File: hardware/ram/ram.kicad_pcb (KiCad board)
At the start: 4 copper layers, 102.9 x 133.3 mm, 64 parts, among them J1 I/O Expansion 1, J2 I/O Expansion 2, J3 DB25_Male, J4 DB37_Male, U1 71V016SA12PHGI, U10 SN74HCS00PWR, U11 SN74HCS00PWR, U12 SN74HCS00PWR, U13 SN74HCS00PWR, U14 SN74HCS00PWR, U15 SN74HCS00PWR, U16 SN74HCS00PWR, U17 SN74HCS00PWR, U18 SN74HCS00PWR, U19 SN74HCS00PWR, U2 SN74HCS00PWR, U20 SN74HCS00PWR, U21 SN74HCS00PWR, U22 SN74HCS00PWR, U23 SN74HCS00PWR, U24 SN74HCS00PWR, U25 SN74HCS00PWR, U26 SN74HCS00PWR, U27 SN74HCS00PWR, U28 SN74HCS00PWR, U29 SN74HCS00PWR, U3 SN74HCS00PWR, U30 SN74HCS00PWR, U31 SN74HCS00PWR, U32 SN74HCS00PWR, U33 SN74HCS00PWR, U34 SN74HCS00PWR, U35 SN74HCS00PWR, U36 SN74HCS00PWR, U37 SN74HCS00PWR, U38 SN74HCS00PWR, U39 SN74HCS00PWR, U4 SN74HCS00PWR, U40 SN74HCS00PWR, U41 SN74HCS00PWR, U42 SN74HCS00PWR, U43 SN74HCS00PWR, U44 SN74HCS00PWR, U45 SN74HCS00PWR, U46 SN74HCS00PWR, U47 SN74HCS00PWR, U48 SN74HCS00PWR, U49 SN74HCS00PWR, U5 SN74LVC541APWR, U50 SN74HCS00PWR, U51 SN74HCS00PWR, U52 SN74HCS00PWR, U53 SN74HCS00PWR, U54 SN74HCS00PWR, U6 SN74LVC541APWR, U7 SN74HCS00PWR, U8 SN74HCS00PWR, U9 SN74HCS00PWR

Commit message: All boards as fabbed at v1.0
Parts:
- added G***: LOGO, nandirl logo:logo_sm, F.Cu at (224.8, 16.5)

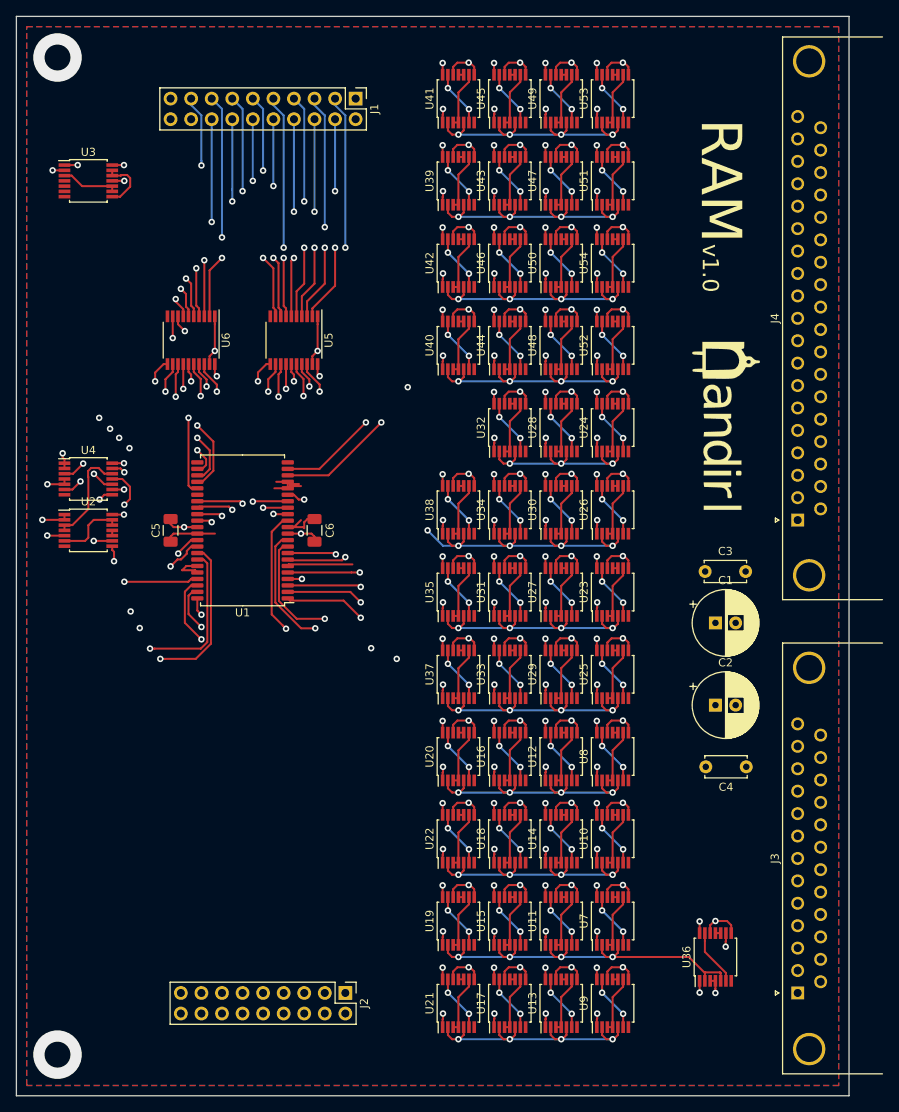
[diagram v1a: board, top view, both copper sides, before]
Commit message: RAM board rework complete. Added COTS latch chips and Teensy 4.1 peripheral + magjack for ethernet.
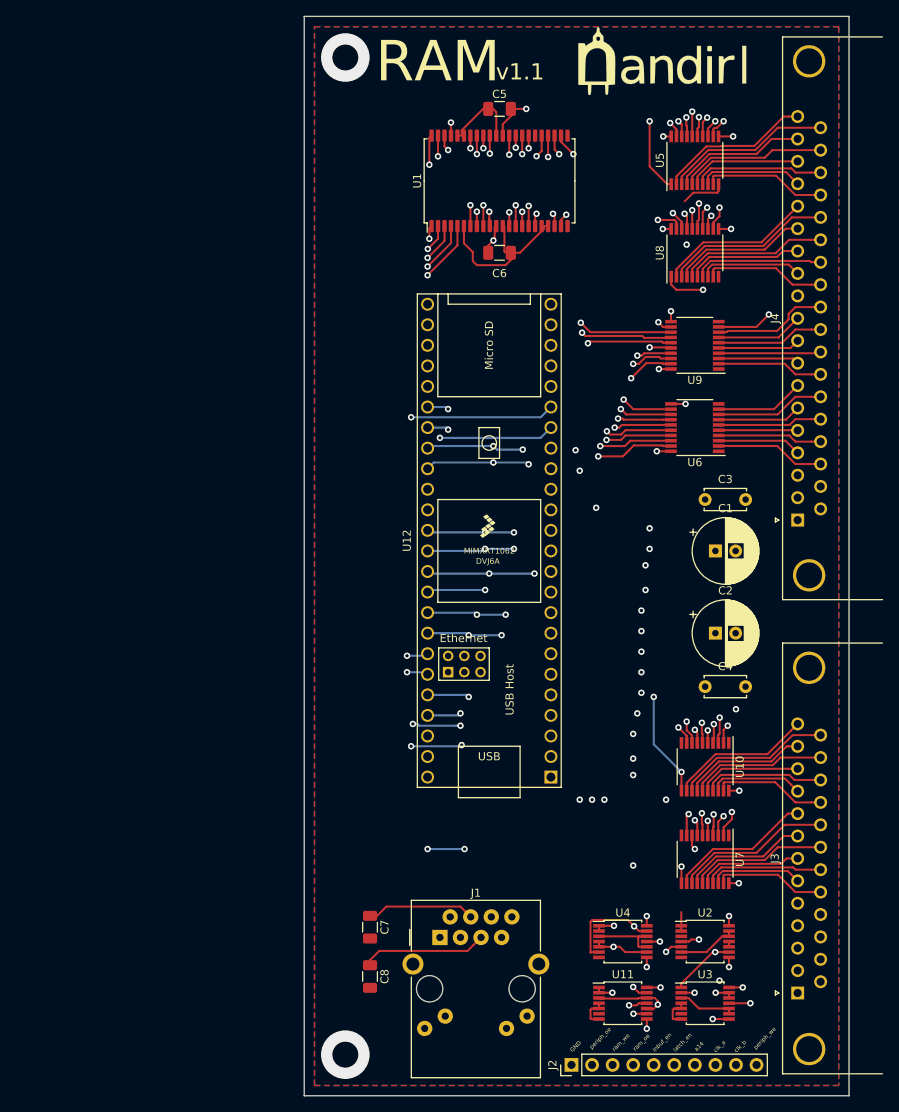
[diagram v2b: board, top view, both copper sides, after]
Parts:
- removed U13, U14, U15, U16, U17, U18, U19, U20, U21, U22, U23, U24, U25, U26, U27, U28, U29, U30, U31, U32, U33, U34, U35, U36, U37, U38, U39, U40, U41, U42, U43, U44, U45, U46, U47, U48, U49, U50, U51, U52, U53, U54: SN74HCS00PWR, Package_SO:TSSOP-14_4.4x5mm_P0.65mm
- added C7: 0.1uF, Capacitor_SMD:C_1206_3216Metric, F.Cu at (180.8, 78.2)
- added C8: 0.1uF, Capacitor_SMD:C_1206_3216Metric, F.Cu at (180.8, 84.3)
- J1: value I/O Expansion 1 -> RJ45_Amphenol_RJMG1BD3B8K1ANR; footprint Connector_PinHeader_2.54mm:PinHeader_2x10_P2.54mm_Vertical -> Connector_RJ:RJ45_Amphenol_RJMG1BD3B8K1ANR
- J2: value I/O Expansion 2 -> Conn_01x10_Male; footprint Connector_PinHeader_2.54mm:PinHeader_2x09_P2.54mm_Vertical -> Connector_PinHeader_2.54mm:PinHeader_1x10_P2.54mm_Vertical
- U10, U7, U8, U9: value SN74HCS00PWR -> 74LCX573FT; footprint Package_SO:TSSOP-14_4.4x5mm_P0.65mm -> Package_SO:TSSOP-20_4.4x6.5mm_P0.65mm
- U12: value SN74HCS00PWR -> Teensy4.1; footprint Package_SO:TSSOP-14_4.4x5mm_P0.65mm -> nandirl logo:Teensy41
- U5, U6: value SN74LVC541APWR -> 74LCX573FT
- moved U3 127.0 mm to (222.2, 87.6)
- moved J1 104.2 mm to (189.5, 79.5), turned to 0 degrees
- moved U2 91.6 mm to (222.2, 80.0)
- moved U4 87.3 mm to (212.1, 80.0)
- moved U9 81.9 mm to (221.0, 6.35), turned to 180 degrees
- moved C5 66.1 mm to (196.8, -22.9), turned to 0 degrees
- moved U6 63.2 mm to (221.0, 16.5), turned to 180 degrees
- moved U8 63.1 mm to (221.0, -5.08)
- moved U5 54.3 mm to (221.0, -16.5), turned to 90 degrees
- moved U1 53.6 mm to (196.8, -14.0), turned to 90 degrees
- moved G*** 45.8 mm to (217.2, -28.7), turned to 0 degrees
- moved C6 41.2 mm to (196.8, -5.08), turned to 0 degrees
- moved J2 29.3 mm to (205.7, 95.2), turned to 90 degrees
- moved U12 28.1 mm to (195.6, 30.5)
- moved U10 14.5 mm to (222.2, 58.4), turned to 270 degrees
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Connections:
- J1 pad 13: a10 -> Net-(J1-Pad13)
- J2 pad 1: io_0 -> GND
- J2 pad 10: io_9 -> periph_we
- J2 pad 2: io_1 -> periph_oe
- J2 pad 3: io_2 -> ram_we
- J2 pad 4: io_3 -> ram_oe
- J2 pad 5: io_4 -> inbuf_en
- J2 pad 6: io_5 -> latch_en
- J2 pad 7: io_6 -> a14
- J2 pad 8: io_7 -> clk_a
- J2 pad 9: io_8 -> clk_b
- U10 pad 1: io_8 -> GND
- U10 pad 10: Net-(U10-Pad10) -> GND
- U10 pad 11: Net-(U10-Pad10) -> latch_en
- U10 pad 12: out_8 -> out_15
- U10 pad 13: Net-(U10-Pad13) -> out_14
- U10 pad 14: +3V3 -> out_13
- U10 pad 2: latch_en -> io_8
- U10 pad 3: Net-(U10-Pad3) -> io_9
- U10 pad 4: Net-(U10-Pad3) -> io_10
- U10 pad 5: latch_en -> io_11
- U10 pad 6: Net-(U10-Pad13) -> io_12
- U10 pad 7: GND -> io_13
- U10 pad 8: out_8 -> io_14
- U10 pad 9: Net-(U10-Pad3) -> io_15
- U11 pad 1: io_5 -> clk_b
- U11 pad 10: Net-(U11-Pad10) -> latch_en
- U11 pad 11: Net-(U11-Pad10) -> periph_oe
- U11 pad 12: out_5 -> latch_en
- U11 pad 13: Net-(U11-Pad13) -> a14
- U11 pad 2: latch_en -> clk_b
- U11 pad 3: Net-(U11-Pad3) -> latch_en
- U11 pad 4: Net-(U11-Pad3) -> GND
- U11 pad 5: latch_en -> GND
- U11 pad 6: Net-(U11-Pad13) -> Net-(U11-Pad6)
- U11 pad 8: out_5 -> ram_oe
- U11 pad 9: Net-(U11-Pad3) -> /not_a14
- U12 pad 1: io_13 -> GND
- U12 pad 10: Net-(U12-Pad10) -> a8
- U12 pad 11: Net-(U12-Pad10) -> a9
- U12 pad 12: out_13 -> a10
- U12 pad 13: Net-(U12-Pad13) -> a11
- U12 pad 14: +3V3 -> a12
- U12 pad 2: latch_en -> a0
- U12 pad 3: Net-(U12-Pad3) -> a1
- U12 pad 4: Net-(U12-Pad3) -> a2
- U12 pad 5: latch_en -> a3
- U12 pad 6: Net-(U12-Pad13) -> a4
- U12 pad 7: GND -> a5
- U12 pad 8: out_13 -> a6
- U12 pad 9: Net-(U12-Pad3) -> a7
- U2 pad 1: a14 -> GND
- U2 pad 2: a14 -> GND
- U2 pad 3: /not_a14 -> Net-(U2-Pad3)
- U2 pad 4: /not_a14 -> clk_b
- U3 pad 4: Net-(U3-Pad4) -> GND
- U3 pad 5: Net-(U3-Pad5) -> GND
- U4 pad 11: ram_oe -> ram_we
- U4 pad 12: /not_a14 -> Net-(U4-Pad10)
- U4 pad 13: latch_en -> /not_a14
- U4 pad 4: clk_b -> a14
- U4 pad 5: clk_b -> a14
- U4 pad 6: latch_en -> /not_a14
- U4 pad 8: ram_we -> periph_we
- U4 pad 9: clk_b -> a14
- U5 pad 11: io_7 -> latch_en
- U5 pad 12: io_6 -> io_7
- U5 pad 13: io_5 -> io_6
- U5 pad 14: io_4 -> io_5
- U5 pad 15: io_3 -> io_4
- U5 pad 16: io_2 -> io_3
- U5 pad 17: io_1 -> io_2
- U5 pad 18: io_0 -> io_1
- U5 pad 19: inbuf_en -> io_0
- U5 pad 2: /input_latch/out0 -> in_0
- U5 pad 3: /input_latch/out1 -> in_1
- U5 pad 4: /input_latch/out2 -> in_2
- U5 pad 5: /input_latch/out3 -> in_3
- U5 pad 6: /input_latch/out4 -> in_4
- U5 pad 7: /input_latch/out5 -> in_5
- U5 pad 8: /input_latch/out6 -> in_6
- U5 pad 9: /input_latch/out7 -> in_7
- U6 pad 1: inbuf_en -> GND
- U6 pad 11: io_15 -> latch_en
- U6 pad 12: io_14 -> a7
- U6 pad 13: io_13 -> a6
- U6 pad 14: io_12 -> a5
- U6 pad 15: io_11 -> a4
- U6 pad 16: io_10 -> a3
- U6 pad 17: io_9 -> a2
- U6 pad 18: io_8 -> a1
- U6 pad 19: inbuf_en -> a0
- U6 pad 2: /input_latch/out8 -> addr_0
- U6 pad 3: /input_latch/out9 -> addr_1
- U6 pad 4: /input_latch/out10 -> addr_2
- U6 pad 5: /input_latch/out11 -> addr_3
- U6 pad 6: /input_latch/out12 -> addr_4
- U6 pad 7: /input_latch/out13 -> addr_5
- U6 pad 8: /input_latch/out14 -> addr_6
- U6 pad 9: /input_latch/out15 -> addr_7
- U7 pad 1: io_4 -> GND
- U7 pad 10: Net-(U7-Pad10) -> GND
- U7 pad 11: Net-(U7-Pad10) -> latch_en
- U7 pad 12: out_4 -> out_7
- U7 pad 13: Net-(U7-Pad13) -> out_6
- U7 pad 14: +3V3 -> out_5
- U7 pad 2: latch_en -> io_0
- U7 pad 3: Net-(U7-Pad3) -> io_1
- U7 pad 4: Net-(U7-Pad3) -> io_2
- U7 pad 5: latch_en -> io_3
- U7 pad 6: Net-(U7-Pad13) -> io_4
- U7 pad 7: GND -> io_5
- U7 pad 8: out_4 -> io_6
- U7 pad 9: Net-(U7-Pad3) -> io_7
- U8 pad 1: io_12 -> inbuf_en
- U8 pad 10: Net-(U8-Pad10) -> GND
- U8 pad 11: Net-(U8-Pad10) -> latch_en
- U8 pad 12: out_12 -> io_15
- U8 pad 13: Net-(U8-Pad13) -> io_14
- U8 pad 14: +3V3 -> io_13
- U8 pad 2: latch_en -> in_8
- U8 pad 3: Net-(U8-Pad3) -> in_9
- U8 pad 4: Net-(U8-Pad3) -> in_10
- U8 pad 5: latch_en -> in_11
- U8 pad 6: Net-(U8-Pad13) -> in_12
- U8 pad 7: GND -> in_13
- U8 pad 8: out_12 -> in_14
- U8 pad 9: Net-(U8-Pad3) -> in_15
- U9 pad 1: io_0 -> GND
- U9 pad 10: Net-(U9-Pad10) -> GND
- U9 pad 11: Net-(U9-Pad10) -> latch_en
- U9 pad 12: out_0 -> load
- U9 pad 13: Net-(U9-Pad13) -> a14
- U9 pad 14: +3V3 -> a13
- U9 pad 2: latch_en -> addr_8
- U9 pad 3: Net-(U9-Pad3) -> addr_9
- U9 pad 4: Net-(U9-Pad3) -> addr_10
- U9 pad 5: latch_en -> addr_11
- U9 pad 6: Net-(U9-Pad13) -> addr_12
- U9 pad 7: GND -> addr_13
- U9 pad 8: out_0 -> addr_14
- U9 pad 9: Net-(U9-Pad3) -> load_in
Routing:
- net latch_en: track 618.7 -> 144.7 mm, vias 50 -> 8
- net ram_oe: track 24.3 -> 138.6 mm, vias 2 -> 4
- net load: track 209.9 -> 99.7 mm, vias 2 -> 3
- net inbuf_en: track 54.9 -> 161.0 mm, vias 3 -> 4
- net periph_we: track 0.00 -> 102.7 mm, vias 0 -> 3
- net periph_oe: track 0.00 -> 92.9 mm, vias 0 -> 2
- net ram_we: track 29.8 -> 121.4 mm, vias 2 -> 3
- net load_in: track 17.0 -> 94.8 mm
- net /input_latch/out3: track 68.8 -> 0.00 mm, vias 2 -> 0
- net /input_latch/out11: track 67.5 -> 0.00 mm, vias 2 -> 0
- net /input_latch/out7: track 65.6 -> 0.00 mm, vias 2 -> 0
- net /input_latch/out15: track 64.9 -> 0.00 mm, vias 2 -> 0
- net +3V3: track 85.3 -> 23.2 mm, vias 55 -> 12
- net /input_latch/out2: track 61.5 -> 0.00 mm, vias 2 -> 0
- net /input_latch/out10: track 60.9 -> 0.00 mm, vias 2 -> 0
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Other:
- board size 102.9 x 133.3 mm -> 67.3 x 133.3 mm
- board text added: "GND"
- board text added: "a14"
- board text added: "clk_a"
- board text added: "clk_b"
- board text added: "inbuf_en"
- board text added: "latch_en"
- board text added: "periph_oe"
- board text added: "periph_we"
- board text added: "ram_oe"
- board text added: "ram_we"
- board text added: "v1.1"
- board text removed: "v1.0"
